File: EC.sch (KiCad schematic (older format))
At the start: 38 parts, among them J10 RS232, J2 MICROSD, J6 DEBUG, J8 DEBUG, M1 FAN-4PIN, Q12 FK3303010L, Q13 FK3303010L, Q20 FK3303010L, Q21 FK3303010L, SW3 SW-DIP-4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

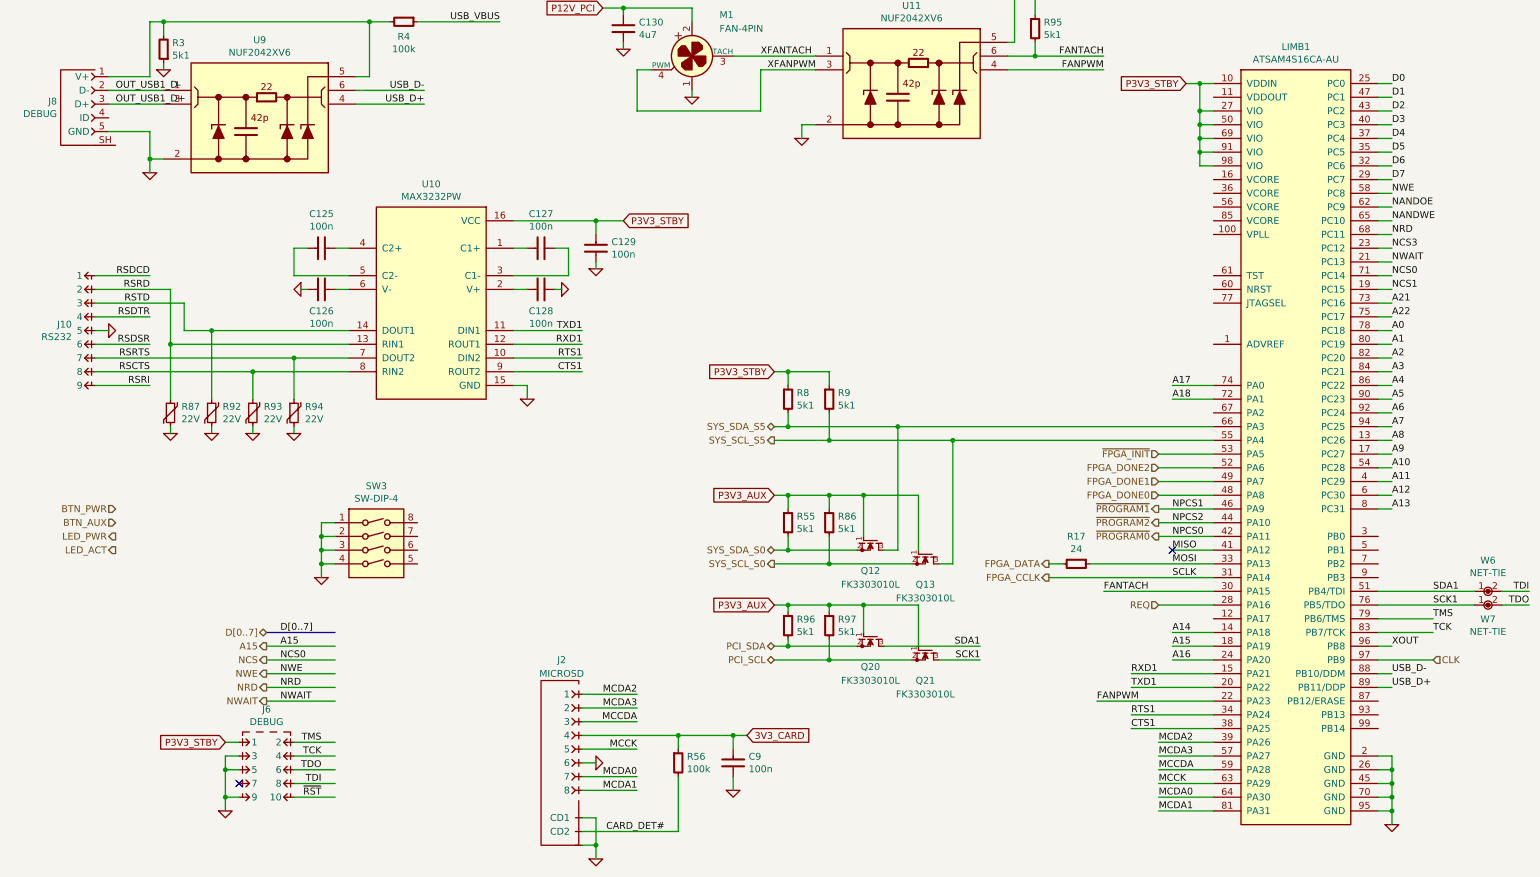
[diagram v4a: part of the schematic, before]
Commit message: Route PCI utility lines
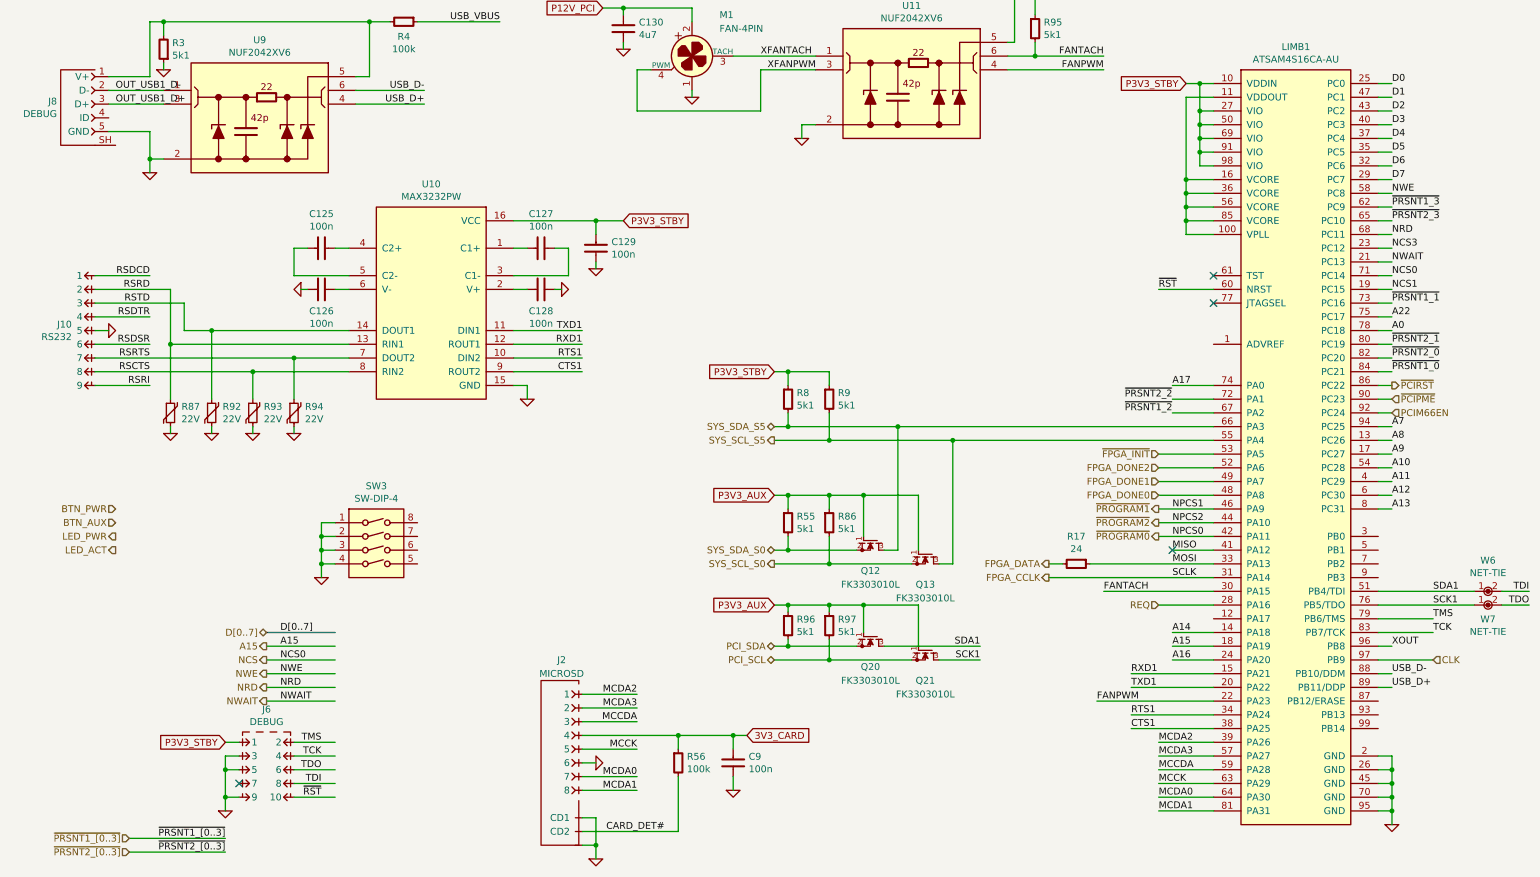
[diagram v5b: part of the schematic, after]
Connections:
- net labels added: PCIM66EN, ~PCIPME, ~PCIRST, ~PRSNT1_0, ~PRSNT1_1, ~PRSNT1_2, ~PRSNT1_3, ~PRSNT1_[0..3], ~PRSNT2_0, ~PRSNT2_1, ~PRSNT2_2, ~PRSNT2_3, ~PRSNT2_[0..3]
- net labels removed: A1, A18, A2, A21, A3, A4, A5, A6, NANDOE, NANDWE
- wire segments 227 -> 238
- no-connect marks 2 -> 4
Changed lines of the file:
@@
 Text Label 10600 3200 0    50   ~ 0
 A0
-Text Label 10600 3300 0    50   ~ 0
-A1
-Text Label 10600 3400 0    50   ~ 0
-A2
-Text Label 10600 3500 0    50   ~ 0
-A3
-Text Label 10600 3600 0    50   ~ 0
-A4
-Text Label 10600 3700 0    50   ~ 0
-A5
-Text Label 10600 3800 0    50   ~ 0
-A6
 Text Label 10600 3900 0    50   ~ 0
 A7
@@
 Text Label 9000 3600 0    50   ~ 0
 A17
-Text Label 9000 3700 0    50   ~ 0
-A18
-Text Label 10600 3000 0    50   ~ 0
-A21
 Text Label 10600 3100 0    50   ~ 0
 A22
@@
 Text Label 10600 2100 0    50   ~ 0
 D7
-Text Label 10600 2300 0    50   ~ 0
-NANDOE
-Text Label 10600 2400 0    50   ~ 0
-NANDWE
 Text Label 10600 2800 0    50   ~ 0
 NCS0
@@
 PCI_SCL
 Connection ~ 6500 5600
+Text HLabel 1400 6900 0    50   Input ~ 0
+~PRSNT1_[0..3]
+Text HLabel 1400 7000 0    50   Input ~ 0
+~PRSNT2_[0..3]
+Text Label 2100 6900 2    50   ~ 0
+~PRSNT1_[0..3]
+Wire Wire Line
+	1400 6900 2100 6900
+Text Label 2100 7000 2    50   ~ 0
+~PRSNT2_[0..3]
+Wire Wire Line
+	1400 7000 2100 7000
+Text Label 10600 3500 0    50   ~ 0
+~PRSNT1_0
+Text Label 10600 3400 0    50   ~ 0
+~PRSNT2_0
+Text Label 10600 3300 0    50   ~ 0
+~PRSNT2_1
+Wire Wire Line
+	9000 3800 9300 3800
+Text Label 10600 3000 0    50   ~ 0
+~PRSNT1_1
+Text Label 9000 3700 2    50   ~ 0
+~PRSNT2_2
+Wire Wire Line
+	9300 1500 9100 1500
+Wire Wire Line
+	9100 1500 9100 2500
+Wire Wire Line
+	9100 2100 9300 2100
+Wire Wire Line
+	9100 2200 9300 2200
+Connection ~ 9100 2100
+Wire Wire Line
+	9100 2300 9300 2300
+Connection ~ 9100 2200
+Wire Wire Line
+	9100 2400 9300 2400
+Connection ~ 9100 2300
+Wire Wire Line
+	9100 2500 9300 2500
+Connection ~ 9100 2400
+NoConn ~ 9300 2800
+Wire Wire Line
+	8900 2900 9300 2900
+NoConn ~ 9300 3000
+Text Label 8900 2900 0    50   ~ 0
+~RST
+Text Label 9000 3800 2    50   ~ 0
+~PRSNT1_2
+Text Label 10600 2400 0    50   ~ 0
+~PRSNT2_3
+Text Label 10600 2300 0    50   ~ 0
+~PRSNT1_3
+Text HLabel 10600 3600 2    50   Output ~ 0
+~PCIRST
+Text HLabel 10600 3700 2    50   Input ~ 0
+~PCIPME
+Text HLabel 10600 3800 2    50   Input ~ 0
+PCIM66EN
 $EndSCHEMATC

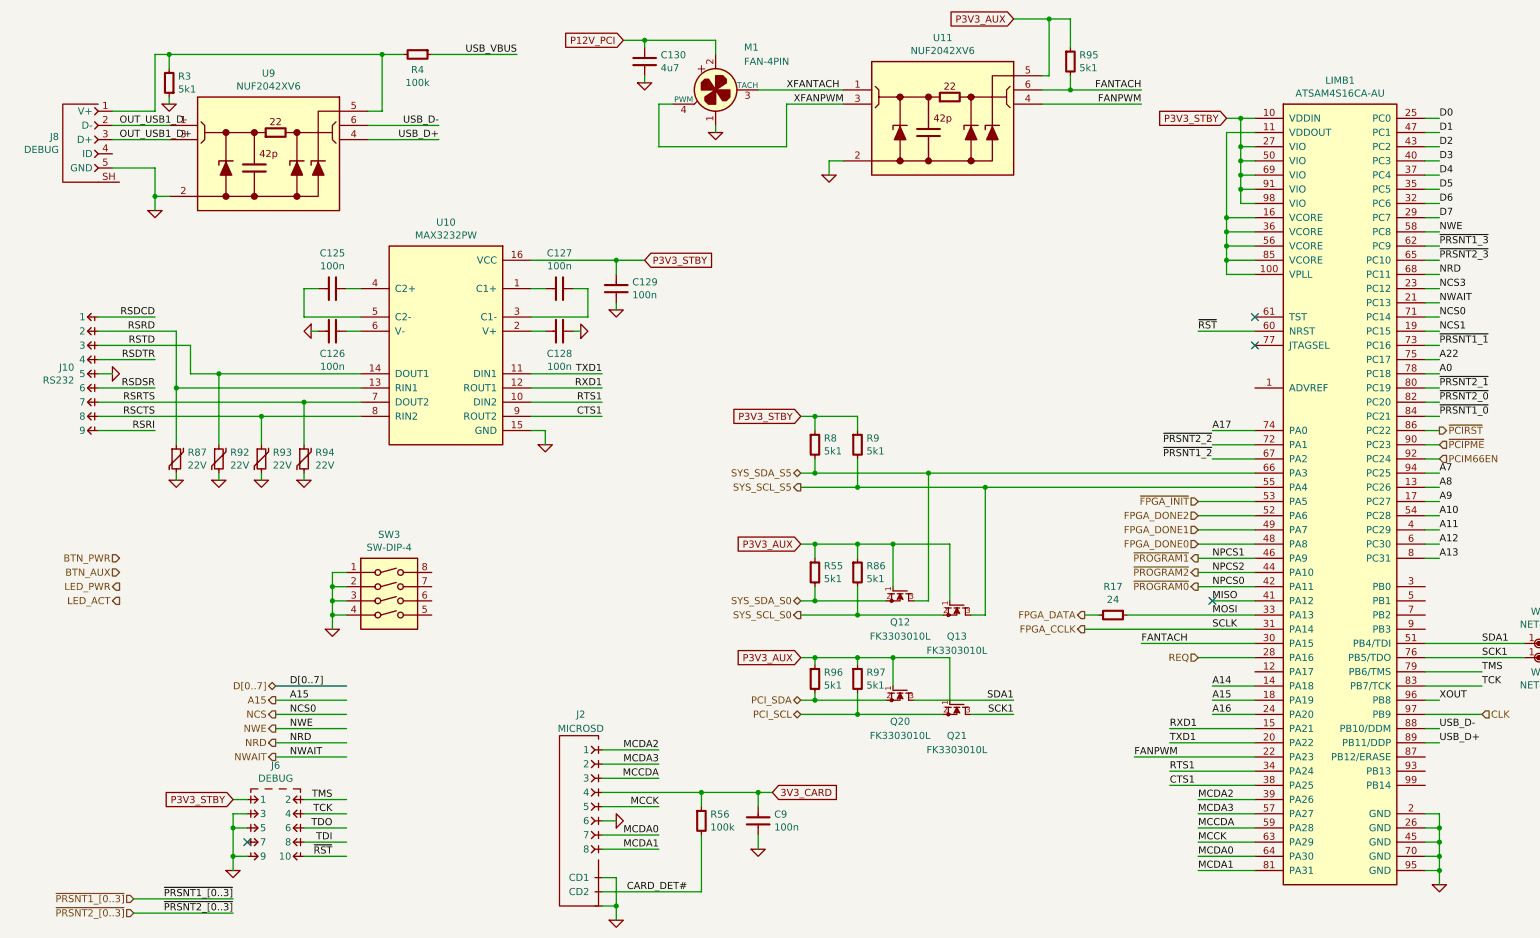
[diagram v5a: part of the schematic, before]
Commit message: Add configuration pullup resistors
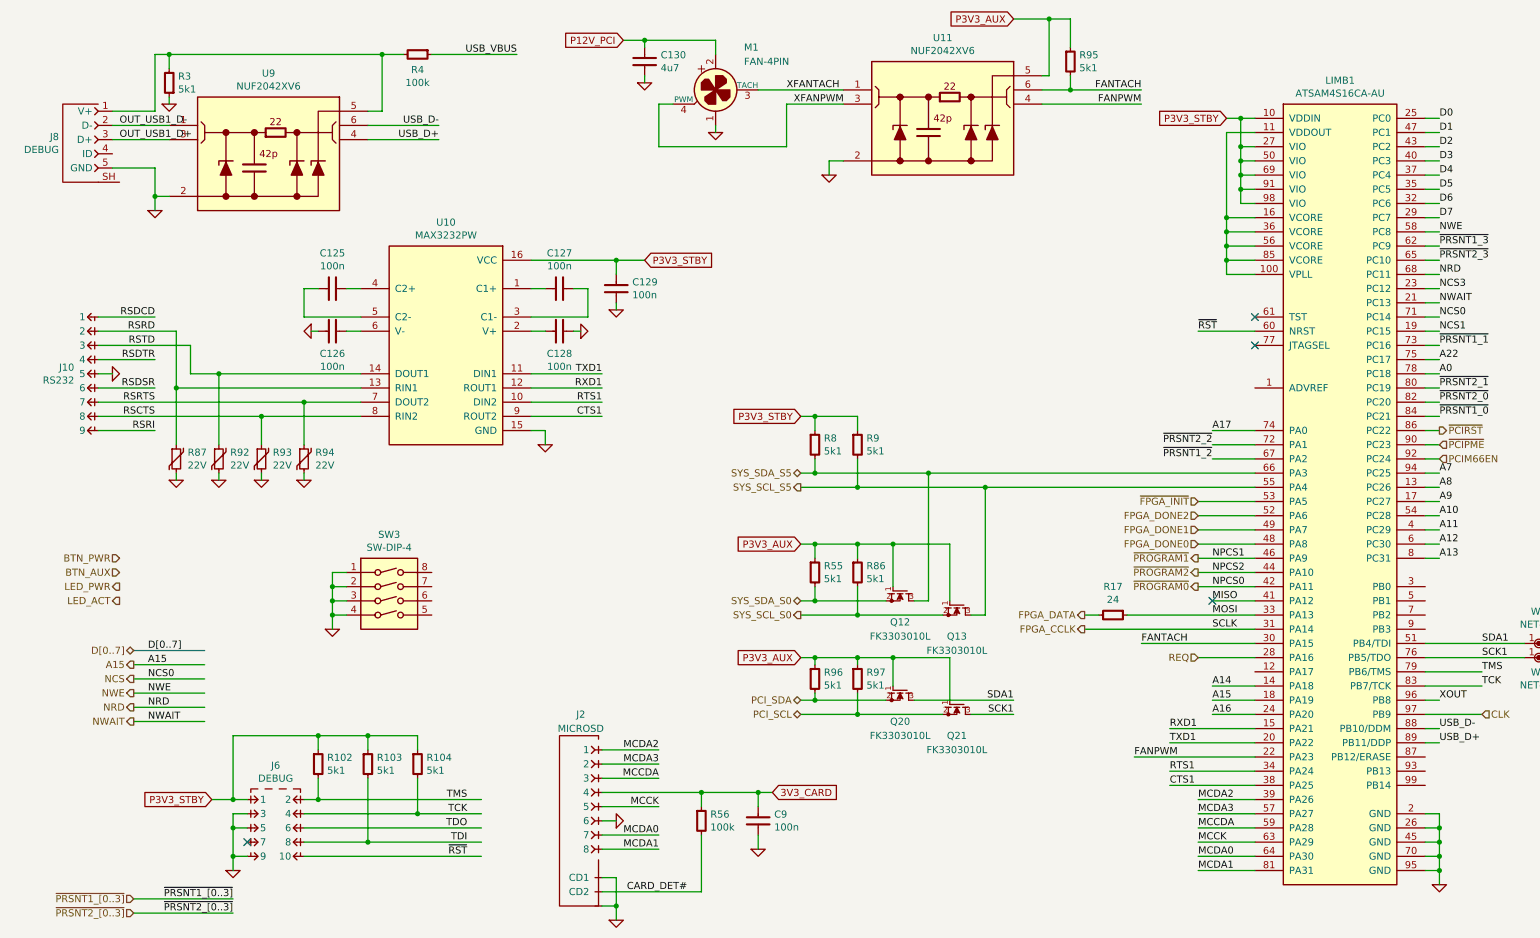
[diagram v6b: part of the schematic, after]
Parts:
- added R102, R103, R104: 5k1, IPC7351-Nominal:RESC1005X40, symbol R-0402
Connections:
- wire segments 238 -> 299

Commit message: Tidy up EC sheet
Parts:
- removed J10: RS232, symbol CONN-100MIL-M-1x9
- removed J8: DEBUG, conn-fci:CONN-10118194-0001LF-FCI, symbol CONN-10118194-0001LF-UUSB-B
- removed SW3: SW-DIP-4, dip-sip:DIP-8, symbol SW-DIP-4
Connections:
- net labels added: RS232_CTS, RS232_RTS, RS232_RX, RS232_TX, SCL0, SDA0, USB_VBSENSE, XUSB_D+, XUSB_D-
- net labels removed: OUT_USB1_D+, OUT_USB1_D-, RSCTS, RSDCD, RSDSR, RSDTR, RSRD, RSRI, RSRTS, RSTD
- wire segments 299 -> 240
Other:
- moved on the sheet: C125, C126, C127, C128, C129, C130, C9, J2, J6, LIMB1, M1, Q12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
